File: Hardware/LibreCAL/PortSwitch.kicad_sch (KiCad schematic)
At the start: 47 parts, among them J1 901-10510-2, J2 901-10510-2, J3 901-10510-2, J4 901-10510-2, U1 PE426462, U2 PE426462, U3 PE426462, U4 PE426462

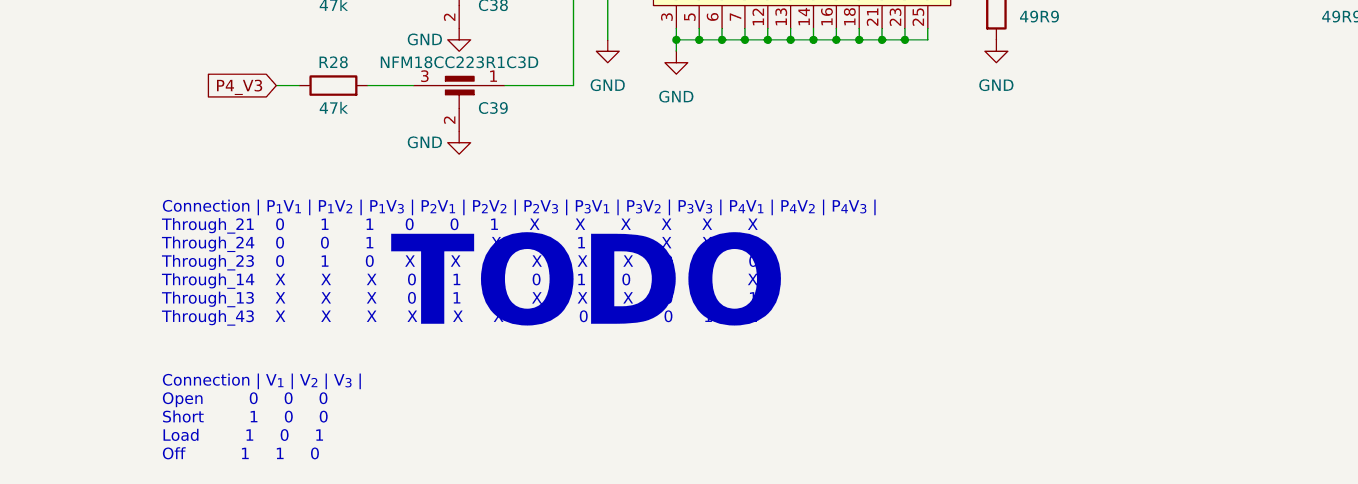
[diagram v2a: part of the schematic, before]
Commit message: replaced bootsel switch, adjusted covers
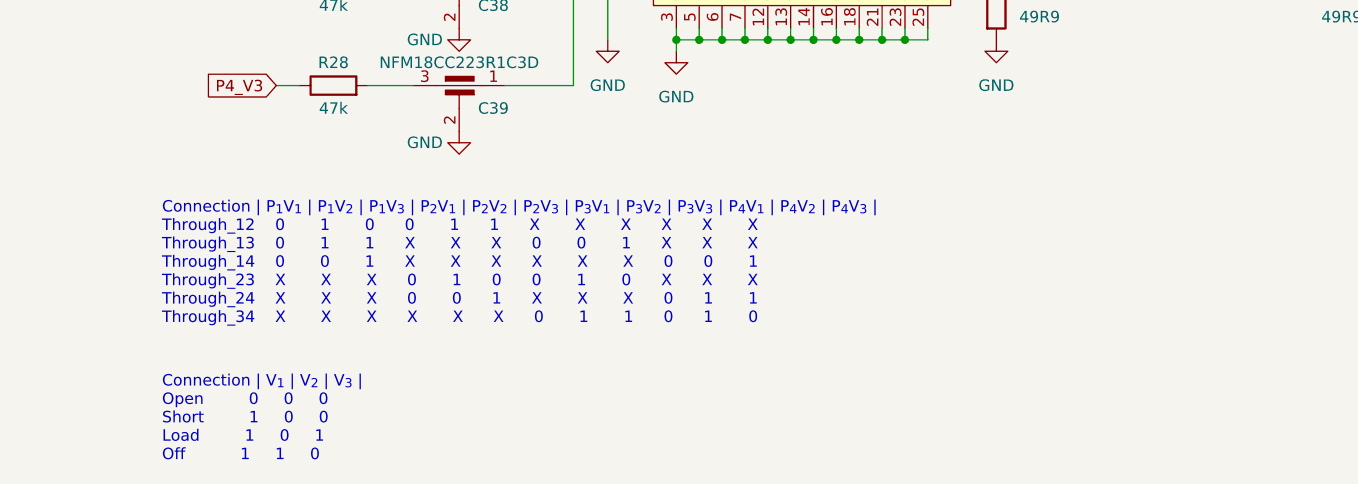
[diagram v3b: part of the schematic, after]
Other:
- note added: "Connection | P_{1}V_{1} | P_{1}V_{2} | P_{1}V_{3} | P_{2}V_{1} | P_{2}V_{2} | P_{2}V_{3} | P_{3}V_{1} | P_{3}V_{2} | P_{3}V_{3} | P_{4}V_{1} | P_{4}V_{2} | P_{4}V_{3} | Through_12 0 1 0 0 1 1 X X X X X X Through_13 0 1 1 X X X 0 0 1 X X X Through_14 0 0 1 X X X X X X 0 0 1 Through_23 X X X 0 1 0 0 1 0 X X X Through_24 X X X 0 0 1 X X X 0 1 1 Through_34 X X X X X X 0 1 1 0 1 0"
- note removed: "Connection | P_{1}V_{1} | P_{1}V_{2} | P_{1}V_{3} | P_{2}V_{1} | P_{2}V_{2} | P_{2}V_{3} | P_{3}V_{1} | P_{3}V_{2} | P_{3}V_{3} | P_{4}V_{1} | P_{4}V_{2} | P_{4}V_{3} | Through_21 0 1 1 0 0 1 X X X X X X Through_24 0 0 1 X X X 0 1 1 X X X Through_23 0 1 0 X X X X X X 0 1 0 Through_14 X X X 0 1 0 0 1 0 X X X Through_13 X X X 0 1 1 X X X 0 0 1 Through_43 X X X X X X 0 0 1 0 1 1"
- note removed: "TODO"
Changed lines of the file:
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@@
     (stroke (width 0) (type default) (color 0 0 0 0))
   )
-  (text "Connection | P_{1}V_{1} | P_{1}V_{2} | P_{1}V_{3} | P_{2}V_{1} | P_{2}V_{2} | P_{2}V_{3} | P_{3}V_{1} | P_{3}V_{2} | P_{3}V_{3} | P_{4}V_{1} | P_{4}V_{2} | P_{4}V_{3} |\nThrough_21    0       1       1      0       0      1      X       X       X      X      X       X    \nThrough_24    0       0       1      X       X      X      0       1       1      X      X       X    \nThrough_23    0       1       0      X       X      X      X       X       X      0      1       0    \nThrough_14    X       X       X      0       1      0      0       1       0      X      X       X    \nThrough_13    X       X       X      0       1      1      X       X       X      0      0       1    \nThrough_43    X       X       X      X       X      X      0       0       1      0      1       1    "
+  (text "Connection | P_{1}V_{1} | P_{1}V_{2} | P_{1}V_{3} | P_{2}V_{1} | P_{2}V_{2} | P_{2}V_{3} | P_{3}V_{1} | P_{3}V_{2} | P_{3}V_{3} | P_{4}V_{1} | P_{4}V_{2} | P_{4}V_{3} |\nThrough_12    0       1       0      0       1      1      X       X       X      X      X       X    \nThrough_13    0       1       1      X       X      X      0       0       1      X      X       X    \nThrough_14    0       0       1      X       X      X      X       X       X      0      0       1    \nThrough_23    X       X       X      0       1      0      0       1       0      X      X       X    \nThrough_24    X       X       X      0       0      1      X       X       X      0      1       1    \nThrough_34    X       X       X      X       X      X      0       1       1      0      1       0    "
     (at 33.02 173.99 0)
     (effects (font (size 1.27 1.27)) (justify left bottom))
   )
-  (text "TODO" (at 58.42 175.26 0)
-    (effects (font (size 10 10) (thickness 2) bold) (justify left bottom))
-  )
   (text "Connection | V_{1} | V_{2} | V_{3} |\nOpen         0     0     0 \nShort         1     0     0 \nLoad         1     0     1\nOff           1     1     0 "

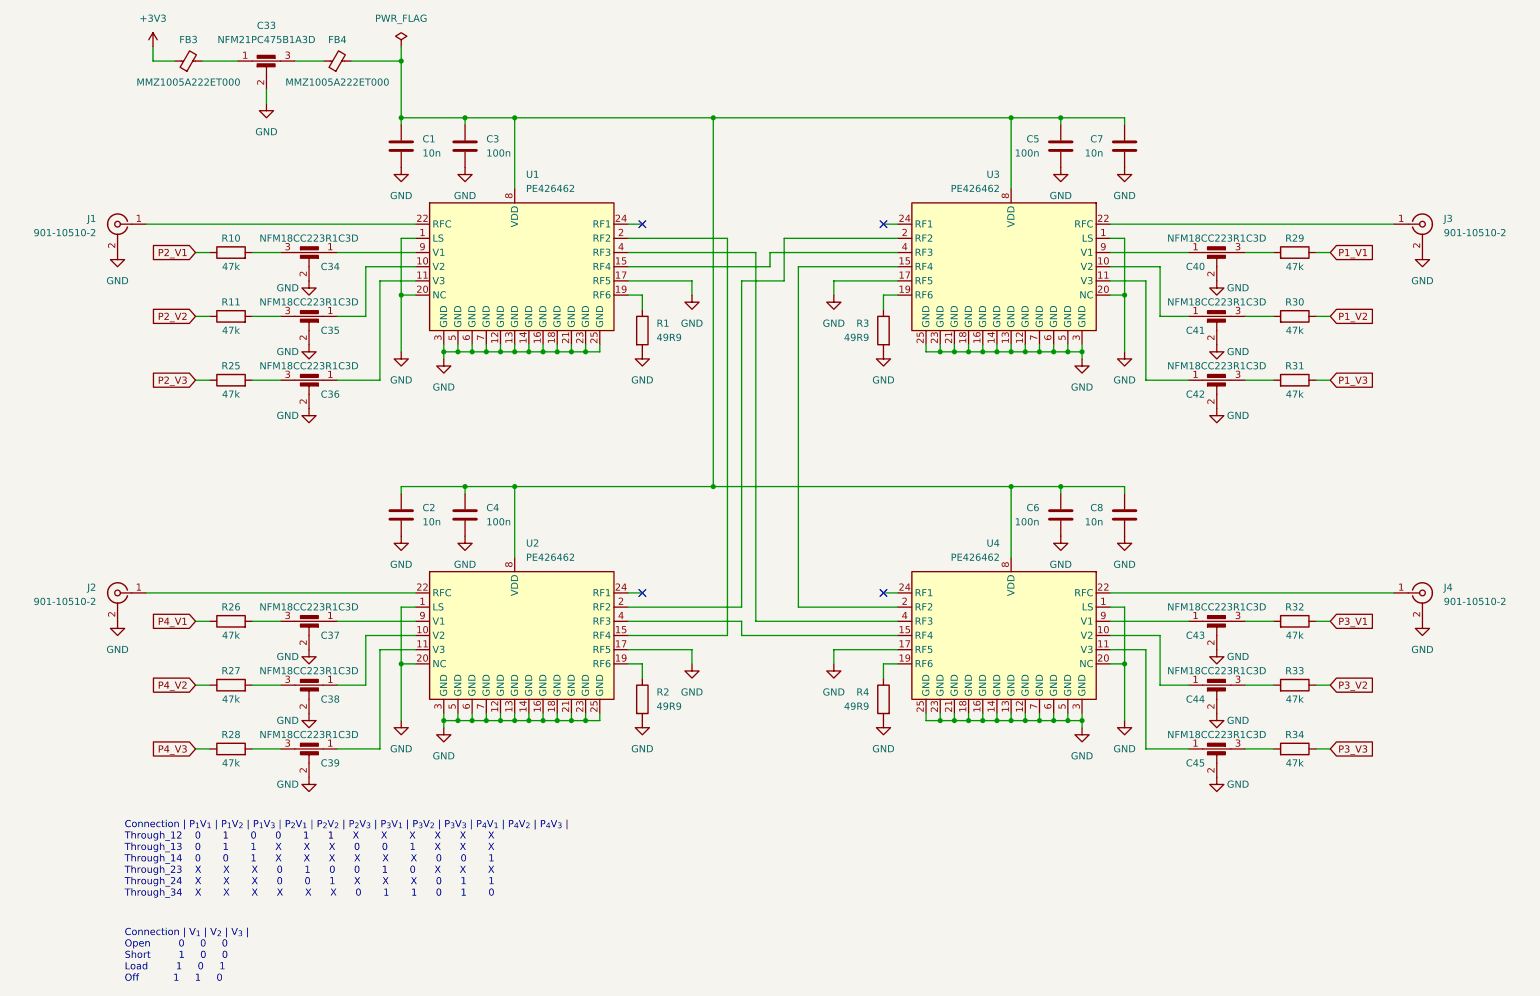
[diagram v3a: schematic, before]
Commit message: Improvements on LibreCAL KiCad: fixed minor errors/labels(cosmetic), improved BOM(Added LCSC_Part), improved Impedance JLCPCB 4Layer JLC7628 1.6mm
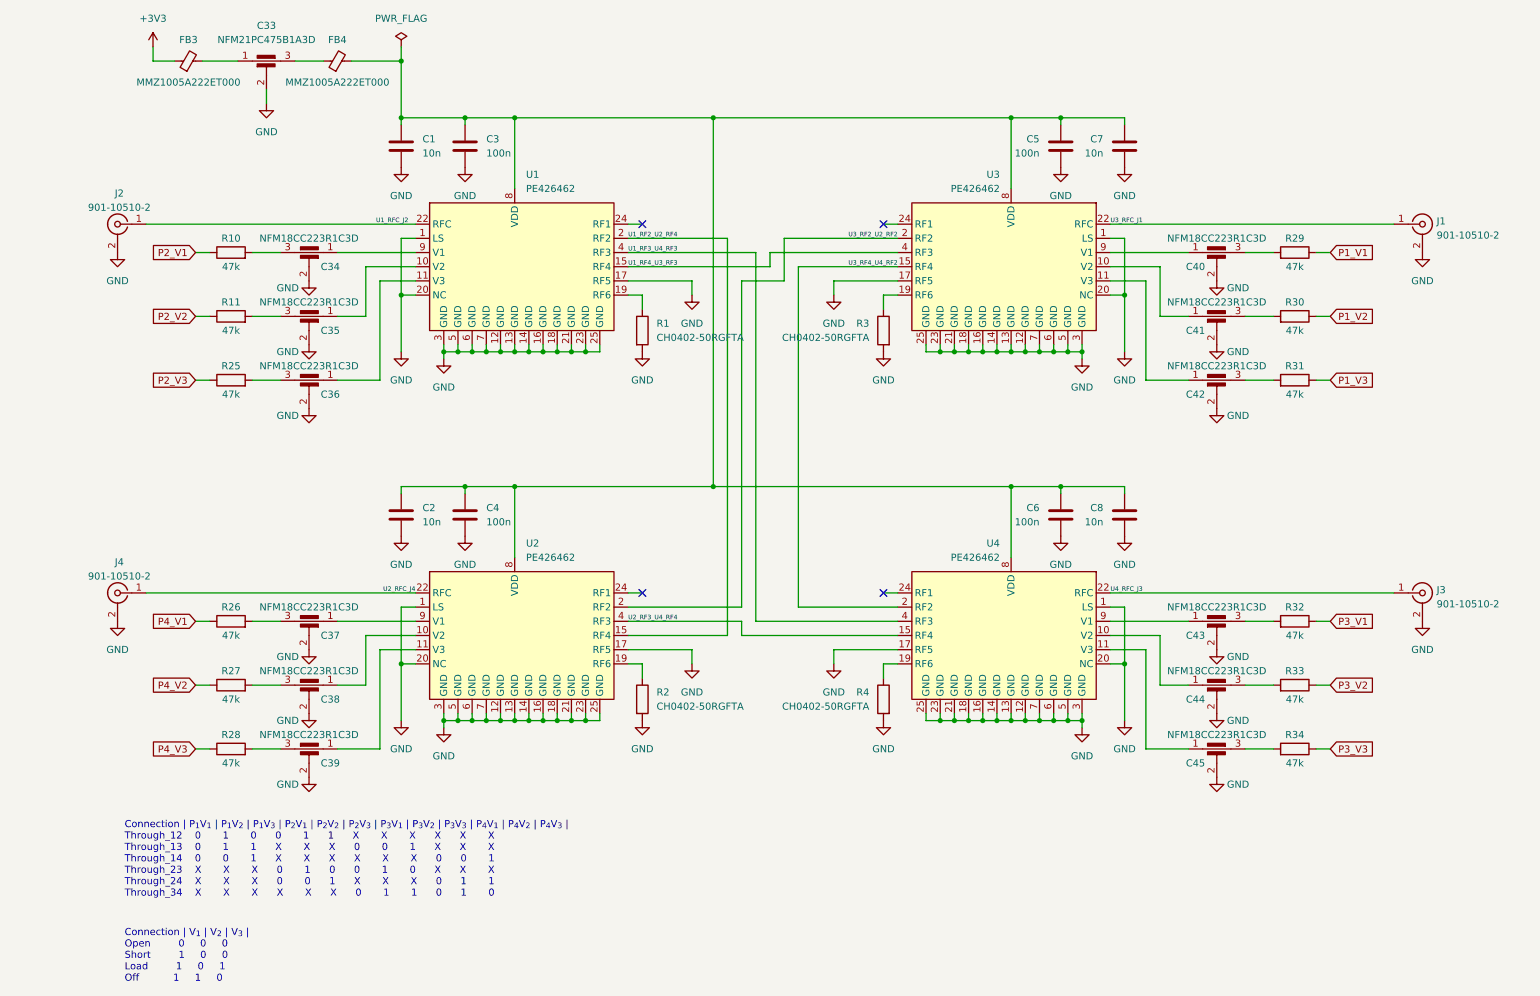
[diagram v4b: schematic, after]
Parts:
- C1, C2, C7, C8: LCSC_Part (none) -> C15195
- C3, C4, C5, C6: LCSC_Part (none) -> C307331
- C33: LCSC_Part (none) -> C96293
- C34, C35, C36, C37, C38, C39, C40, C41, C42, C43, C44, C45: LCSC_Part (none) -> C98102
- FB3, FB4: LCSC_Part (none) -> C275411
- J1: renamed from J3; LCSC_Part (none) -> C3172623
- J2: renamed from J1; LCSC_Part (none) -> C3172623
- J3: renamed from J4; LCSC_Part (none) -> C3172623
- J4: renamed from J2; LCSC_Part (none) -> C3172623
- R1, R2, R3, R4: value 49R9 -> CH0402-50RGFTA; LCSC_Part (none) -> C5349731
- R10, R11, R25, R26, R27, R28, R29, R30, R31, R32, R33, R34: LCSC_Part (none) -> C144757
- U1, U2, U3, U4: LCSC_Part (none) -> C5349078
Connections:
- net U1_RF2_U2_RF4: now reaches U1.2 (RF2), U2.15 (RF4)
- net U3_RF2_U2_RF2: now reaches U2.2 (RF2), U3.2 (RF2)
- net U2_RFC_J4: now reaches J4.1 (In), U2.22 (RFC)
- net U2_RF3_U4_RF4: now reaches U2.4 (RF3), U4.15 (RF4)
- net U4_RFC_J3: now reaches J3.1 (In), U4.22 (RFC)
- net U3_RF4_U4_RF2: now reaches U3.15 (RF4), U4.2 (RF2)
- net U1_RF3_U4_RF3: now reaches U1.4 (RF3), U4.4 (RF3)
- net U1_RF4_U3_RF3: now reaches U1.15 (RF4), U3.4 (RF3)
- net U1_RFC_J2: now reaches J2.1 (In), U1.22 (RFC)
- net U3_RFC_J1: now reaches J1.1 (In), U3.22 (RFC)
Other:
- title: (none) -> LibreCAL
